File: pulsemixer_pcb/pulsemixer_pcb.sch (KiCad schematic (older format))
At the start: 25 parts, among them SW1 Mute Ch4

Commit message: Finished inital schematic, and a little bit of PCB layout.
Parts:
- removed C? (x4): 0.1µ, symbol Device:C
- removed D? (x4): LED, symbol Device:LED
- removed R1, R? (x3): 10K, symbol Device:R
- removed R? (x4): R, symbol Device:R
- removed RV4, RV? (x3): R_POT, symbol Device:R_POT
- removed SHIELD1: ARDUINO_FOOTPRINT, FT:ARDUINO_SHIELD, symbol freetronics_schematic:ARDUINO_FOOTPRINT
- removed SW1, SW? (x3): Mute Ch4, symbol freetronics_schematic:SW_PUSHBUTTON
- added A101: Arduino_Nano_v3.x, pulsemixer_pcb:SHIELD_ARDUINO_NANO, symbol MCU_Module:Arduino_Nano_v3.x
- added C101: 10µ, Capacitors_THT:CP_Radial_D5.0mm_P2.00mm, symbol Device:C
- added D101, D102, D103, D104, D105, D106, D107, D108: DIODE, Diodes_SMD:D_SOD-323_HandSoldering, symbol freetronics_schematic:DIODE
- added D109: LED, LEDs:LED_1206_HandSoldering, symbol Device:LED
- added R101, R102: 4.7K, Resistors_SMD:R_1206_HandSoldering, symbol Device:R
- added R103, R104, R105: 10K, Resistors_SMD:R_1206_HandSoldering, symbol Device:R
- added R106: 150, Resistors_SMD:R_1206_HandSoldering, symbol Device:R
- added RV101: 10K, Resistors_SMD:R_1206_HandSoldering, symbol Device:R_POT
- added SW101: SW_PG_RIGHT, Buttons_Switches_THT:SW_PUSH_6mm, symbol freetronics_schematic:SW_PUSHBUTTON
- added SW102: SW_PG_LEFT, Buttons_Switches_THT:SW_PUSH_6mm, symbol freetronics_schematic:SW_PUSHBUTTON
- added SW103: SW_STRM_DEV, Buttons_Switches_THT:SW_PUSH_6mm, symbol freetronics_schematic:SW_PUSHBUTTON
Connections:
- net labels added: INTA, INTB, LCD_V0, PAGE_LEFT_BTN, PAGE_RIGHT_BTN, SCK, SDA, STRM_DEV, STRM_DEV_LED
- net labels removed: Mute_Btn_Ch1, Mute_Btn_Ch2, Mute_Btn_Ch3, Mute_Btn_Ch4, Mute_LED_Ch1, Mute_LED_Ch2, Mute_LED_Ch3, Mute_LED_Ch4, Vol_Pot_Ch1, Vol_Pot_Ch2, Vol_Pot_Ch3, Vol_Pot_Ch4
- wire segments 85 -> 132
- no-connect marks 0 -> 19
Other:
- note added: "Arduino Nano MCU"
- note added: "LCD Contrast Pot"
- note added: "Master Controls"

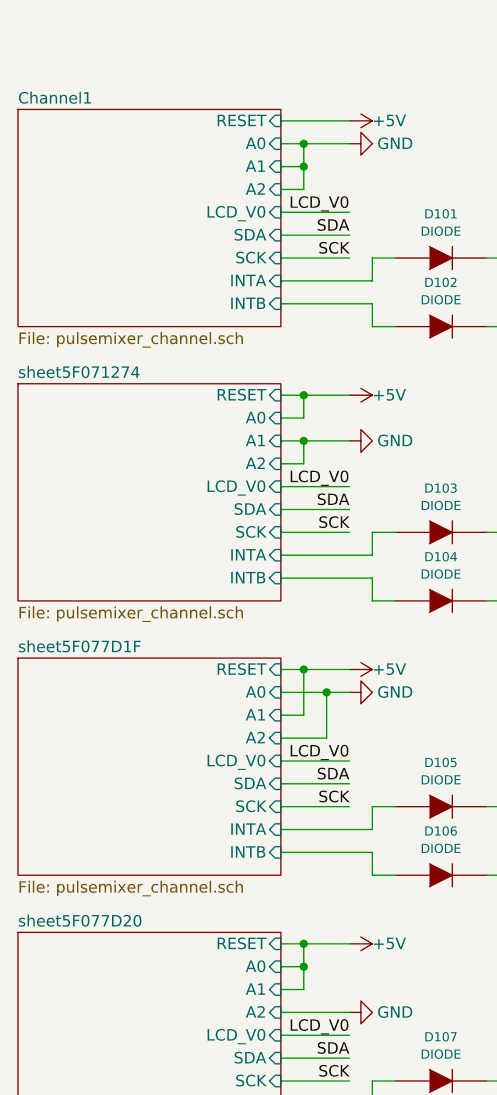
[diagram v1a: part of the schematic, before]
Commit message: Revised schematic after testing rotary encoder.
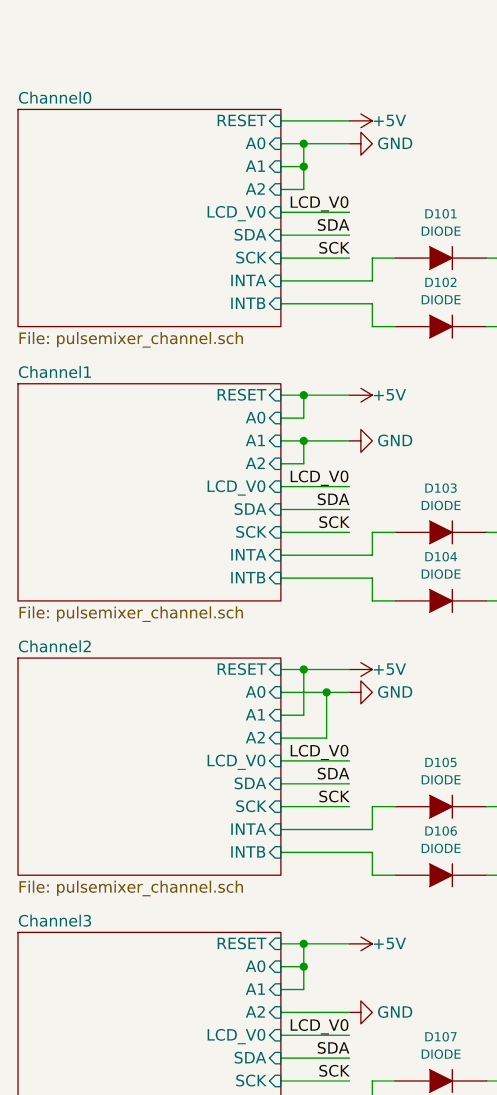
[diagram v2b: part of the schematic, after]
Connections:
- net sheet5F071274/INTA is gone; now on net Channel1/INTA: D103.A
- net sheet5F071274/INTB is gone; now on net Channel1/INTB: D104.A
- net Channel1/INTA: no longer D101.A
- net Channel1/INTB: no longer D102.A
- net sheet5F077D1F/INTA renamed Channel2/INTA
- net sheet5F077D1F/INTB renamed Channel2/INTB
- net sheet5F077D20/INTA renamed Channel3/INTA
- net sheet5F077D20/INTB renamed Channel3/INTB
- new net Channel0/INTA: D101.A
- new net Channel0/INTB: D102.A
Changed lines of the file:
@@
 S 1550 2400 1150 950
 U 5F07127F
-F0 "sheet5F071274" 50
+F0 "Channel1" 50
 F1 "pulsemixer_channel.sch" 50
 F2 "SCK" I R 2700 3050 50
@@
 S 1550 3600 1150 950
 U 5F077D2B
-F0 "sheet5F077D1F" 50
+F0 "Channel2" 50
 F1 "pulsemixer_channel.sch" 50
 F2 "SCK" I R 2700 4250 50
@@
 S 1550 4800 1150 950
 U 5F077D67
-F0 "sheet5F077D20" 50
+F0 "Channel3" 50
 F1 "pulsemixer_channel.sch" 50
 F2 "SCK" I R 2700 5450 50
@@
 S 1550 1200 1150 950
 U 5EF5CDBF
-F0 "Channel1" 50
+F0 "Channel0" 50
 F1 "pulsemixer_channel.sch" 50
 F2 "SCK" I R 2700 1850 50

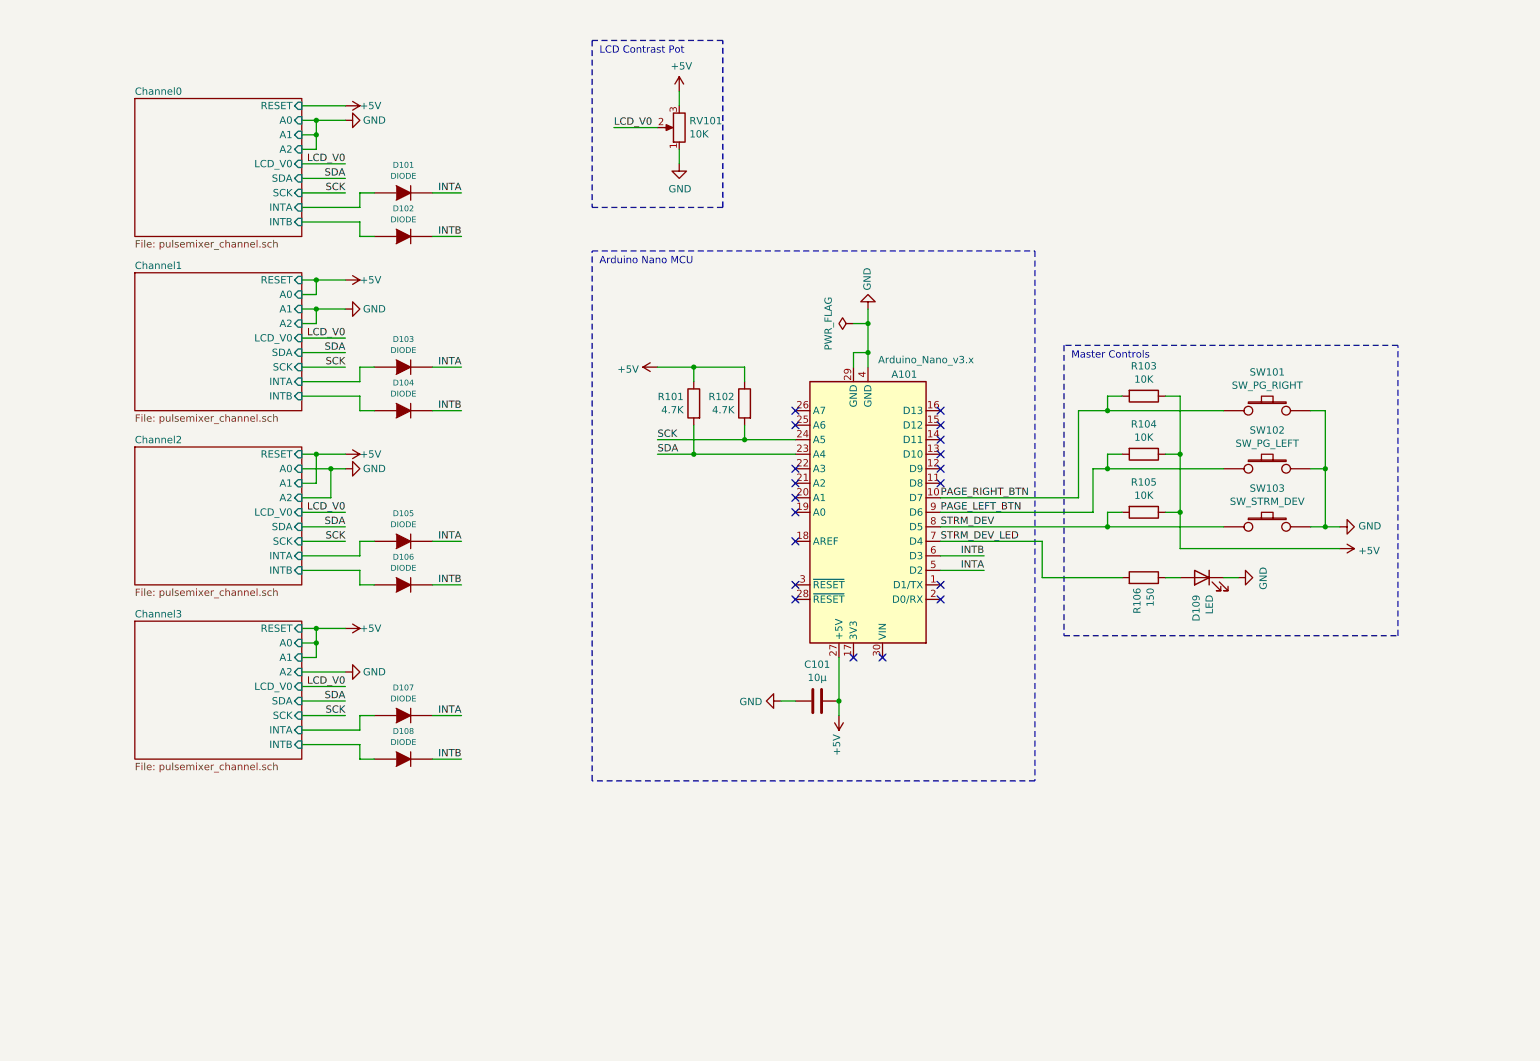
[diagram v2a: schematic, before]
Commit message: Simple reading of rotary encoder through the GPIO expander, with interrupts.
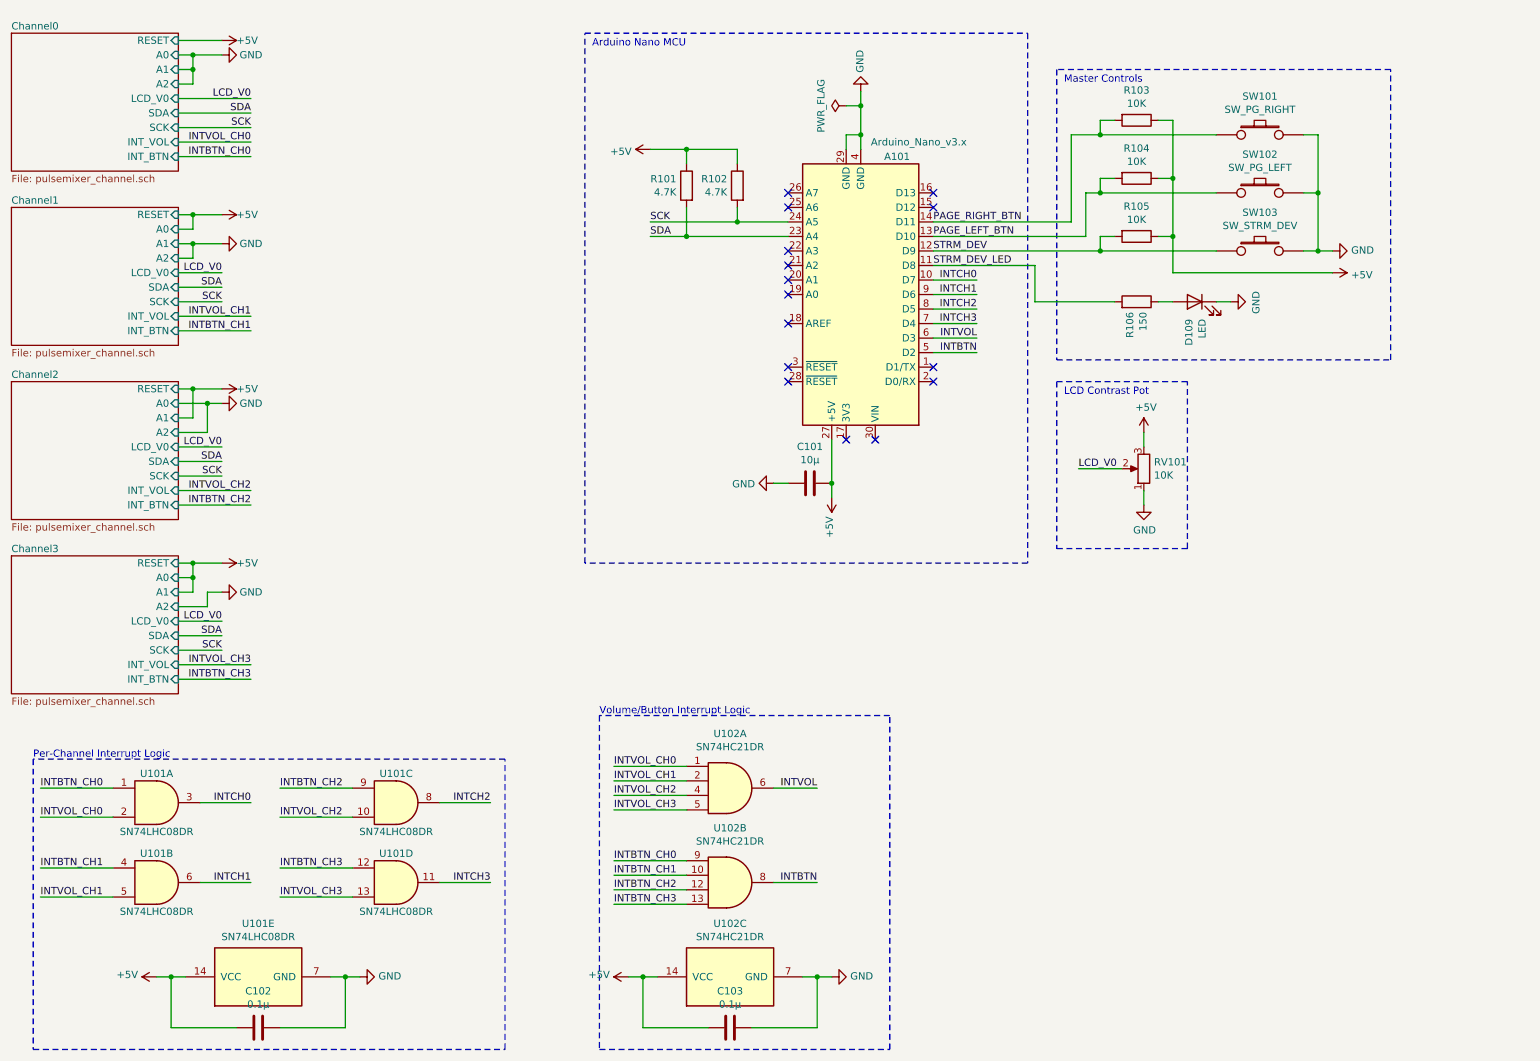
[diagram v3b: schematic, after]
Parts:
- removed D101, D102, D103, D104, D105, D106, D107, D108: DIODE, Diodes_SMD:D_SOD-323_HandSoldering, symbol freetronics_schematic:DIODE
- added C102, C103: 0.1µ, Capacitors_SMD:C_0805_HandSoldering, symbol Device:C
- added U101: SN74LHC08DR, Housings_SOIC:SOIC-14_3.9x8.7mm_Pitch1.27mm, symbol pulsemixer_pcb:SN74LHC08DR
- added U102: SN74HC21DR, Housings_SOIC:SOIC-14_3.9x8.7mm_Pitch1.27mm, symbol pulsemixer_pcb:SN74HC21DR
- RV101: footprint Resistors_SMD:R_1206_HandSoldering -> pulsemixer_pcb:TRIM_3352T-1-103LF
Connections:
- net +5V: now also C102.1, C103.1, U101.14 (VCC), U102.14 (VCC)
- net GND: now also C102.2, C103.2, U101.7 (GND), U102.7 (GND)
- net PAGE_LEFT_BTN: now also A101.13 (D10); no longer A101.9 (D6)
- net PAGE_RIGHT_BTN: now also A101.14 (D11); no longer A101.10 (D7)
- net STRM_DEV: now also A101.12 (D9); no longer A101.8 (D5)
- net STRM_DEV_LED: now also A101.11 (D8); no longer A101.7 (D4)
- net INTA renamed INTBTN
- net INTBTN: now also U102.8
- net INTB renamed INTVOL
- net INTVOL: now also U102.6
- new net INTBTN_CH0: U101.1, U102.9
- new net INTBTN_CH1: U101.4, U102.10
- new net INTBTN_CH2: U101.9, U102.12
- new net INTBTN_CH3: U101.12, U102.13
- new net INTCH0: A101.10 (D7), U101.3
- new net INTCH1: A101.9 (D6), U101.6
- new net INTCH2: A101.8 (D5), U101.8
- new net INTCH3: A101.7 (D4), U101.11
- new net INTVOL_CH0: U101.2, U102.1
- new net INTVOL_CH1: U101.5, U102.2
- new net INTVOL_CH2: U101.10, U102.4
- new net INTVOL_CH3: U101.13, U102.5
- no-connect marks 19 -> 15
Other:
- note added: "Per-Channel Interrupt Logic"
- note added: "Volume/Button Interrupt Logic"
- moved on the sheet: A101, C101, D109, R101, R102, R103, R104, R105, R106, RV101, SW101, SW102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

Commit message: Finished full PCB layout.
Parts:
- removed C101: 10µ, Capacitors_THT:CP_Radial_D5.0mm_P2.00mm, symbol Device:C
- added C101: 100µ, Capacitors_THT:CP_Radial_D8.0mm_P3.50mm, symbol Device:CP
- added C104, C105, C106, C107: 0.1µ, Capacitors_SMD:C_0805_HandSoldering, symbol Device:C
- added D101, D102, D103, D104: D_Schottky, Diodes_SMD:D_1206, symbol Device:D_Schottky
- added D105: LED_GREEN, LEDs:LED_1206_HandSoldering, symbol Device:LED
- added R107: 1K, Resistors_SMD:R_1206, symbol Device:R
- added R108, R109: 10K, Resistors_SMD:R_1206, symbol Device:R
- added R110: 250, Resistors_SMD:R_1206, symbol Device:R
- added R111: 150, Resistors_SMD:R_1206, symbol Device:R
- added U103: 74LVC3G17, Housings_SSOP:SSOP-8_2.95x2.8mm_Pitch0.65mm, symbol 74xGxx:74LVC3G17
- D109: value LED -> LED_GREEN
- R101, R102, R104, R106: footprint Resistors_SMD:R_1206_HandSoldering -> Resistors_SMD:R_1206
- R103, R105: value 10K -> 1K; footprint Resistors_SMD:R_1206_HandSoldering -> Resistors_SMD:R_1206
- SW101: value SW_PG_RIGHT -> SW_PUSH_SPST
- SW102: value SW_PG_LEFT -> SW_PUSH_SPST
- SW103: value SW_STRM_DEV -> SW_PUSH_SPST
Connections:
- net +5V: now also R104.2, C107.2, D104.1 (K), R108.2, R109.2, R110.2, U103.8 (VCC), U103.8 (VCC), U103.8 (VCC); no longer R103.1, R104.1, R105.1
- net GND: now also C101.2, C104.2, C105.2, C106.2, C107.1, D105.1 (K), U103.4 (GND), U103.4 (GND), U103.4 (GND)
- net INTBTN_CH0: now also U101.2; no longer U101.1
- net INTBTN_CH1: now also U101.5; no longer U101.4
- net INTBTN_CH2: now also U101.10; no longer U101.9
- net INTVOL_CH0: now also U101.1; no longer U101.2
- net INTVOL_CH1: now also U101.4; no longer U101.5
- net INTVOL_CH2: now also U101.9; no longer U101.10
- net STRM_DEV: now also A101.14 (D11), U103.7; no longer A101.12 (D9), R105.2, SW103.1
- net at A101.15 (D12): now also R111.2
- removed net PAGE_LEFT_BTN: A101.13 (D10), R104.2, SW102.1
- removed net PAGE_RIGHT_BTN: A101.14 (D11), R103.2, SW101.1
- new net: D103.2 (A), R104.1, R105.1, SW103.1
- new net: C106.1, D103.1 (K), R105.2, U103.1
- new net: D102.2 (A), R107.1, R109.1, SW102.1
- new net: C105.1, D102.1 (K), R107.2, U103.6
- new net: D101.2 (A), R103.1, R108.1, SW101.1
- new net: C104.1, D101.1 (K), R103.2, U103.3
- new net: D105.2 (A), R111.1
- new net: C101.1, D104.2 (A), R110.1
- new net IO_BTN: A101.13 (D10), U103.5
- new net PAGE_BTN: A101.12 (D9), U103.2
- no-connect marks 15 -> 14
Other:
- note added: "Inputs / Outputs"
- note added: "Page"
- note added: "Stream / Device"
- moved on the sheet: D109, R104, R105, R106, SW103
